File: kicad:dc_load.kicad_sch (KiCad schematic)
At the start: 53 parts, among them J2 LCD socket pin, J3 Conn_01x02, J4 Encoder, J5 GPIO expander, J6 ADS1115 ADC, J7 +, J8 -, Q2 IRLZ44N, Q3 IRLZ44N, U2 L7805, U3 ESP32-C3, U4 TL431LP, U5 MCP4725, U6 LM324

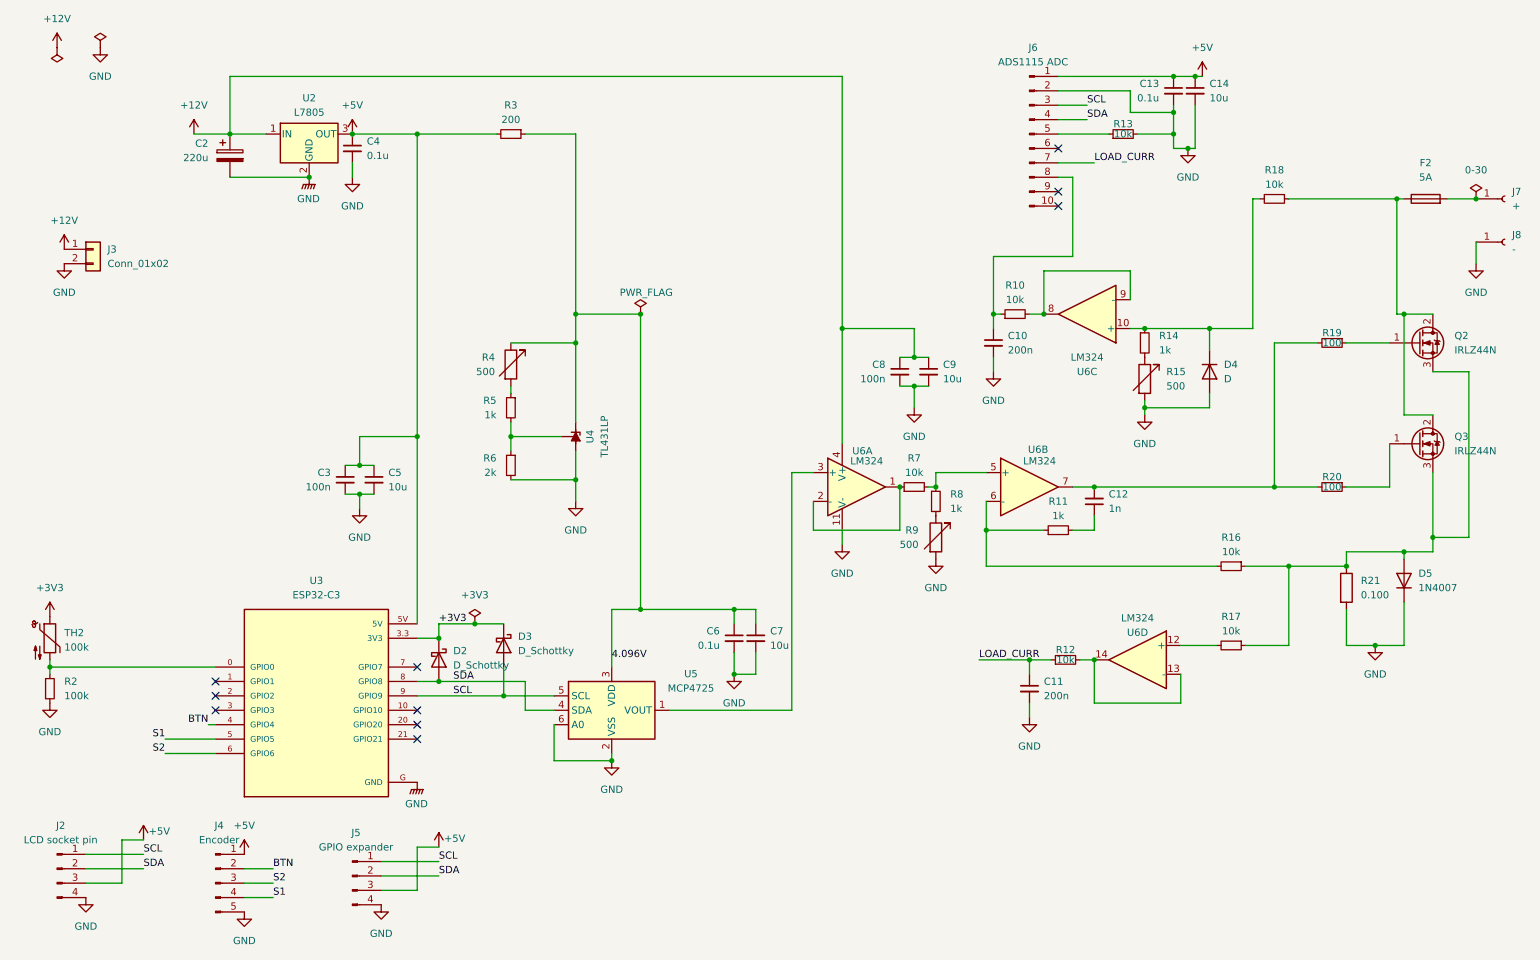
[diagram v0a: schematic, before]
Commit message: Resized PCB and added some caps
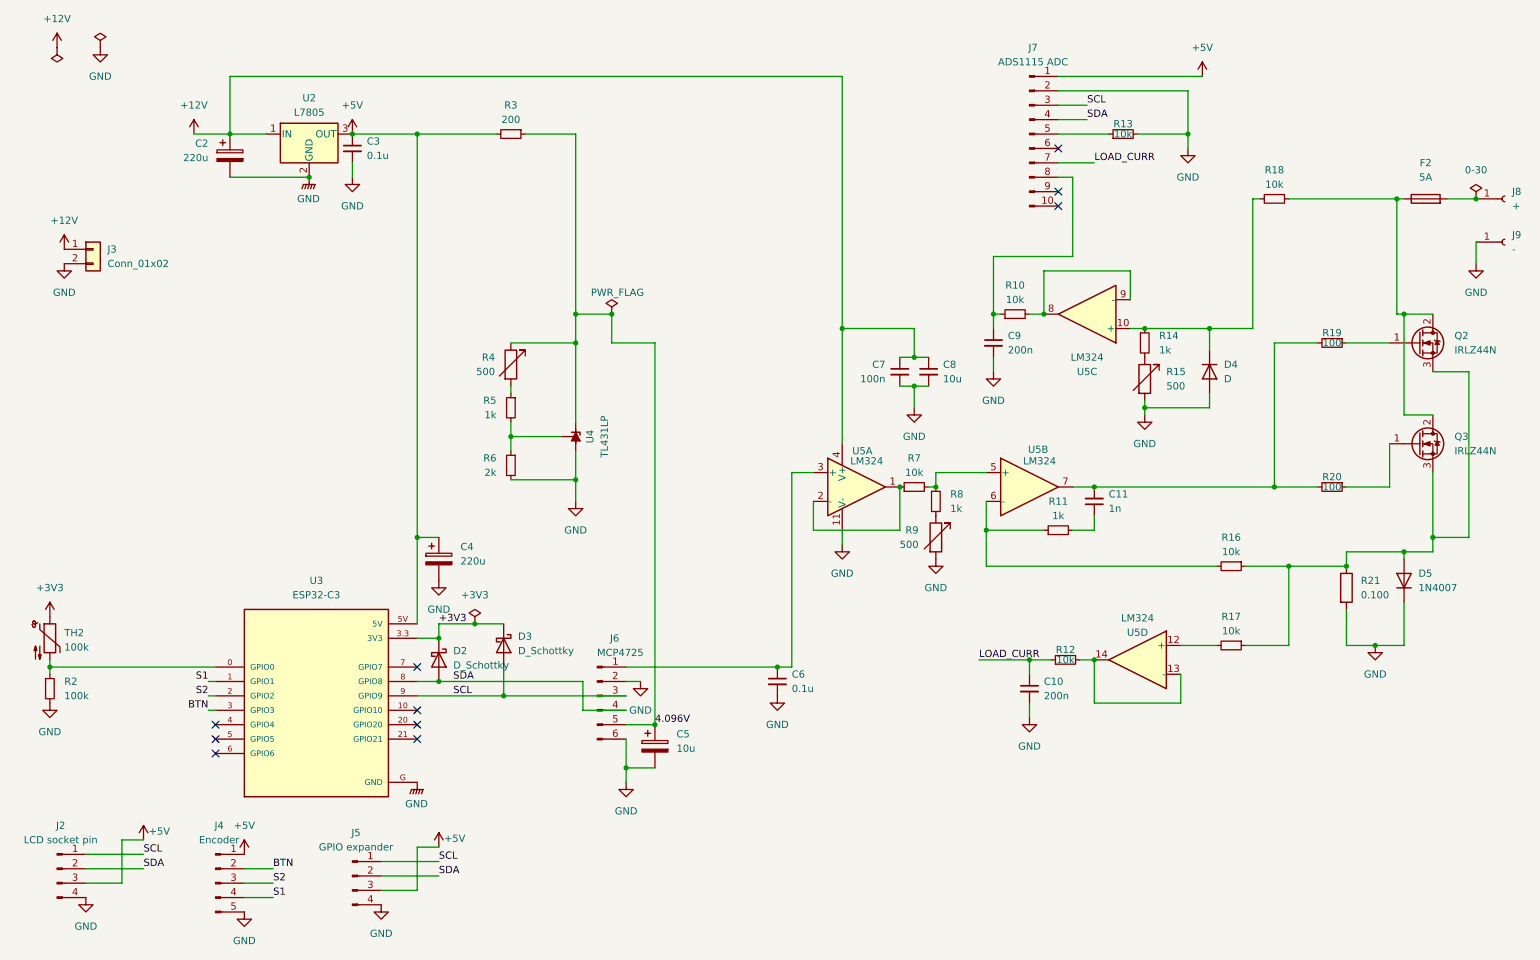
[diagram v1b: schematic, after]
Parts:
- removed C13: 0.1u, Capacitor_THT:C_Disc_D3.0mm_W2.0mm_P2.50mm, symbol Device:C_Small
- removed C14, C5, C7: 10u, Capacitor_THT:CP_Radial_D5.0mm_P2.50mm, symbol Device:C_Small
- removed C3: 100n, Capacitor_THT:C_Disc_D3.0mm_W2.0mm_P2.50mm, symbol Device:C_Small
- removed U5: MCP4725, Package_TO_SOT_SMD:SOT-23-6, symbol Analog_DAC:MCP4725xxx-xCH
- added C4: 220u, symbol Device:C_Polarized
- added C5: 10u, Capacitor_THT:CP_Radial_D5.0mm_P2.50mm, symbol Device:C_Polarized
- added J6: MCP4725, Connector_PinHeader_2.54mm:PinHeader_1x06_P2.54mm_Vertical, symbol Connector:Conn_01x06_Pin
- renumbered C11 to C10, C12 to C11, C4 to C3, C8 to C7, C9 to C8, C10 to C9, J6 to J7, J7 to J8, J8 to J9, U6 to U5
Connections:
- net +5V: now also C4.1
- net 4.096V: now also C5.1, J6.5 (Pin_5); no longer C6.1
- net BTN: now also U3.3 (GPIO3); no longer U3.4 (GPIO4)
- net GND: now also C4.2, C5.2, J6.2 (Pin_2), J6.6 (Pin_6)
- net S1: now also U3.1 (GPIO1); no longer U3.5 (GPIO5)
- net S2: now also U3.2 (GPIO2); no longer U3.6 (GPIO6)
- net SCL: now also J6.3 (Pin_3)
- net SDA: now also J6.4 (Pin_4)
- net at U5.3 (+): now also C6.1, J6.1 (Pin_1)
